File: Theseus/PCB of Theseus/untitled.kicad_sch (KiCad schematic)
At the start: 20 parts, among them J1 TB001-500-04BE, J4 TB003-500-P06BE, J8 TB003-500-P06BE, Q1 NX3020NAK,215, Q2 NX3020NAK,215

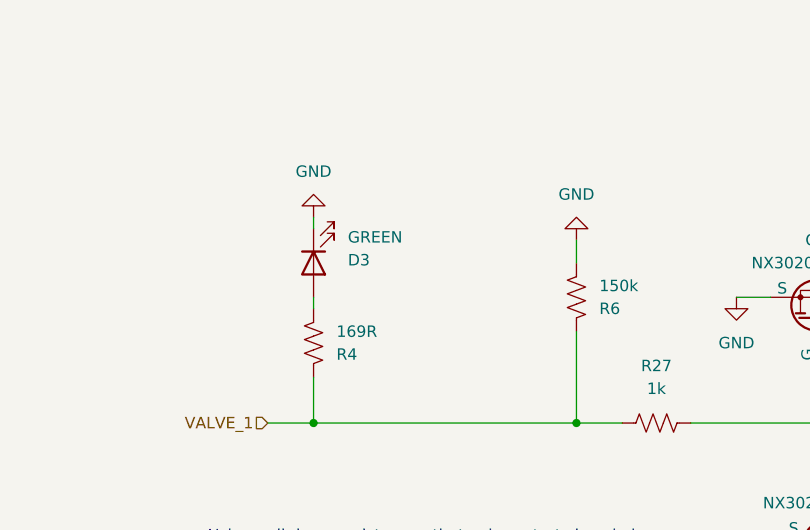
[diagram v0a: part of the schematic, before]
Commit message: Fixes V3
- Copied Ferrite Bead P/N from processor
- Added external oscillator
- Made status LED pins pull-down
- Copied processor programming header
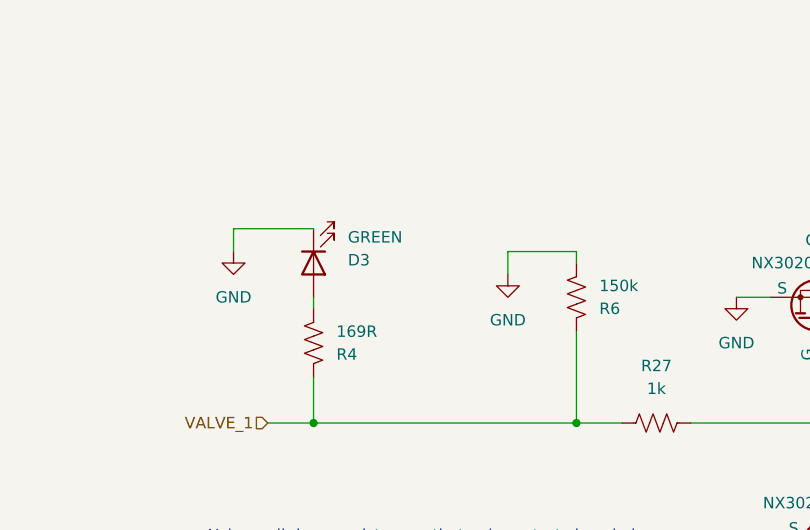
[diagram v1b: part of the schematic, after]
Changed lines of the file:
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@@
 	(wire
 		(pts
-			(xy 180.34 48.26) (xy 180.34 45.72)
+			(xy 172.72 46.99) (xy 172.72 49.53)
 		)
 		(stroke
@@
 	(wire
 		(pts
-			(xy 151.13 43.18) (xy 151.13 44.45)
+			(xy 142.24 46.99) (xy 142.24 44.45)
+		)
+		(stroke
+			(width 0)
+			(type default)
+		)
+	)
+	(wire
+		(pts
+			(xy 142.24 44.45) (xy 151.13 44.45)
 		)
 		(stroke
@@
 	(wire
 		(pts
+			(xy 180.34 46.99) (xy 180.34 48.26)
+		)
+		(stroke
+			(width 0)
+			(type default)
+		)
+	)
+	(wire
+		(pts
 			(xy 219.71 54.61) (xy 219.71 60.96)
 		)
@@
 		(pts
 			(xy 227.33 52.07) (xy 254 52.07)
+		)
+		(stroke
+			(width 0)
+			(type default)
+		)
+	)
+	(wire
+		(pts
+			(xy 172.72 46.99) (xy 180.34 46.99)
 		)
 		(stroke
@@
 	(symbol
 		(lib_id "power:GND")
-		(at 180.34 45.72 0)
-		(mirror x)
+		(at 172.72 49.53 0)
+		(mirror y)
 		(unit 1)
 		(exclude_from_sim no)
@@
 		(on_board yes)
 		(dnp no)
-		(fields_autoplaced yes)
 		(property "Reference" "#PWR06"
-			(at 180.34 39.37 0)
+			(at 172.72 55.88 0)
 			(effects
 				(font
@@
 		)
 		(property "Value" "GND"
-			(at 180.34 40.64 0)
+			(at 172.72 54.61 0)
 			(effects
 				(font
@@
 		)
 		(property "Footprint" ""
-			(at 180.34 45.72 0)
+			(at 172.72 49.53 0)
 			(effects
 				(font
@@
 		)
 		(property "Datasheet" ""
-			(at 180.34 45.72 0)
+			(at 172.72 49.53 0)
 			(effects
 				(font
@@
 		)
 		(property "Description" "Power symbol creates a global label with name \"GND\" , ground"
-			(at 180.34 45.72 0)
+			(at 172.72 49.53 0)
 			(effects
 				(font
@@
 	(symbol
 		(lib_id "power:GND")
-		(at 151.13 43.18 0)
-		(mirror x)
+		(at 142.24 46.99 0)
 		(unit 1)
 		(exclude_from_sim no)
@@
 		(on_board yes)
 		(dnp no)
-		(fields_autoplaced yes)
 		(property "Reference" "#PWR012"
-			(at 151.13 36.83 0)
+			(at 142.24 53.34 0)
 			(effects
 				(font
@@
 		)
 		(property "Value" "GND"
-			(at 151.13 38.1 0)
+			(at 142.24 52.07 0)
 			(effects
 				(font
@@
 		)
 		(property "Footprint" ""
-			(at 151.13 43.18 0)
+			(at 142.24 46.99 0)
 			(effects
 				(font
@@
 		)
 		(property "Datasheet" ""
-			(at 151.13 43.18 0)
+			(at 142.24 46.99 0)
 			(effects
 				(font
@@
 		)
 		(property "Description" "Power symbol creates a global label with name \"GND\" , ground"
-			(at 151.13 43.18 0)
-			(effects
-				(font
+			(at 142.24 46.99 0)
+			(effects
+				(font

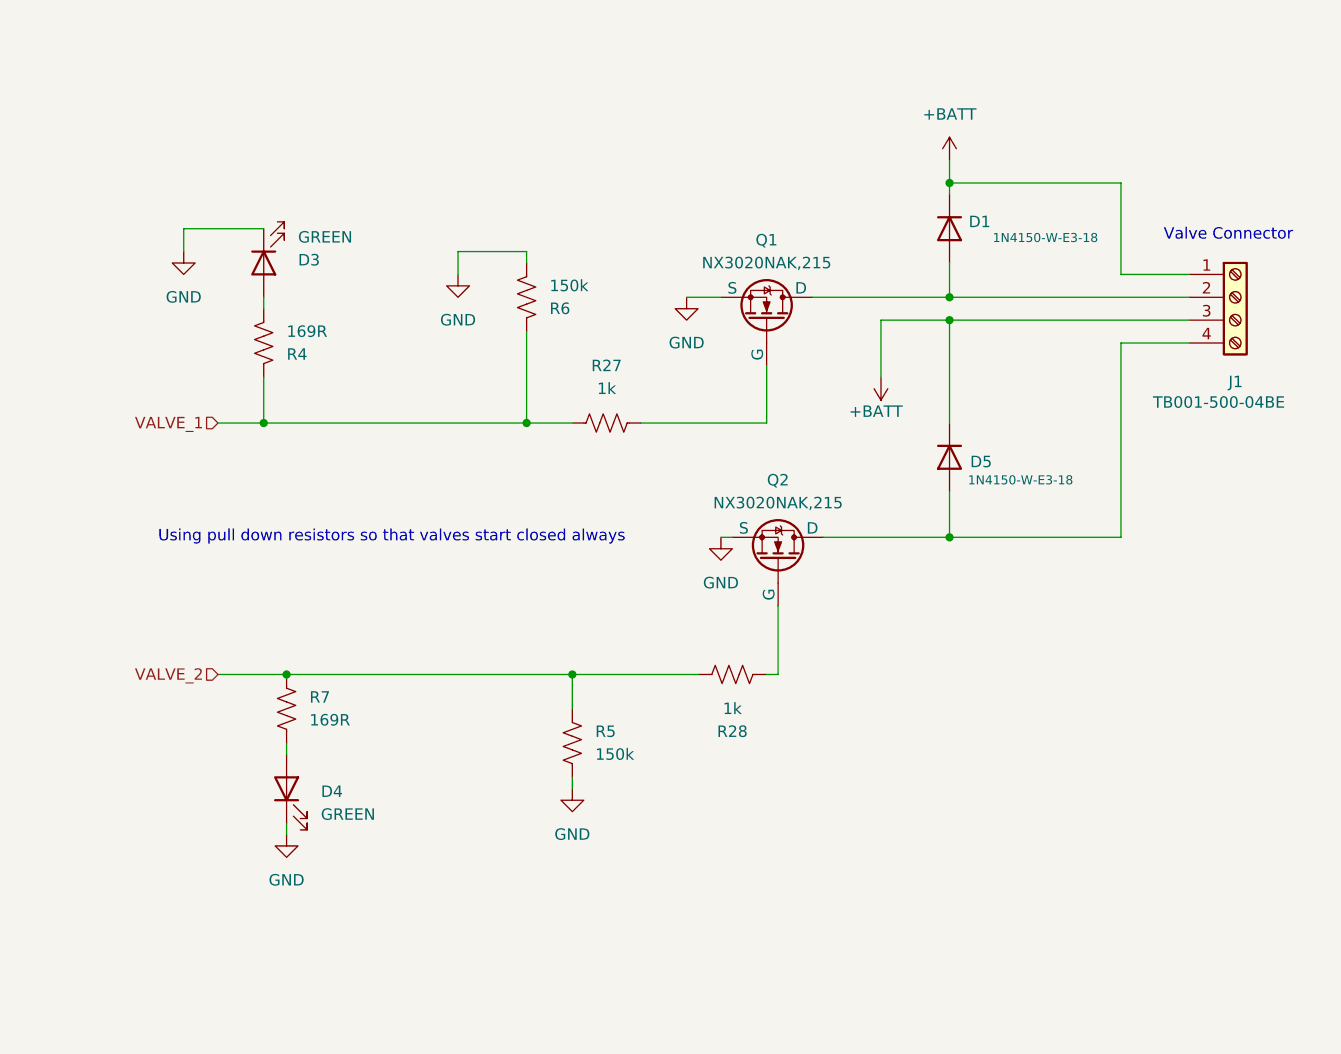
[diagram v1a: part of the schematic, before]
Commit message: NMOS and Diode Update
Updated Diode and NMOS to support 1A max. Fixed valve state LED to draw from BATT instead of MCU.
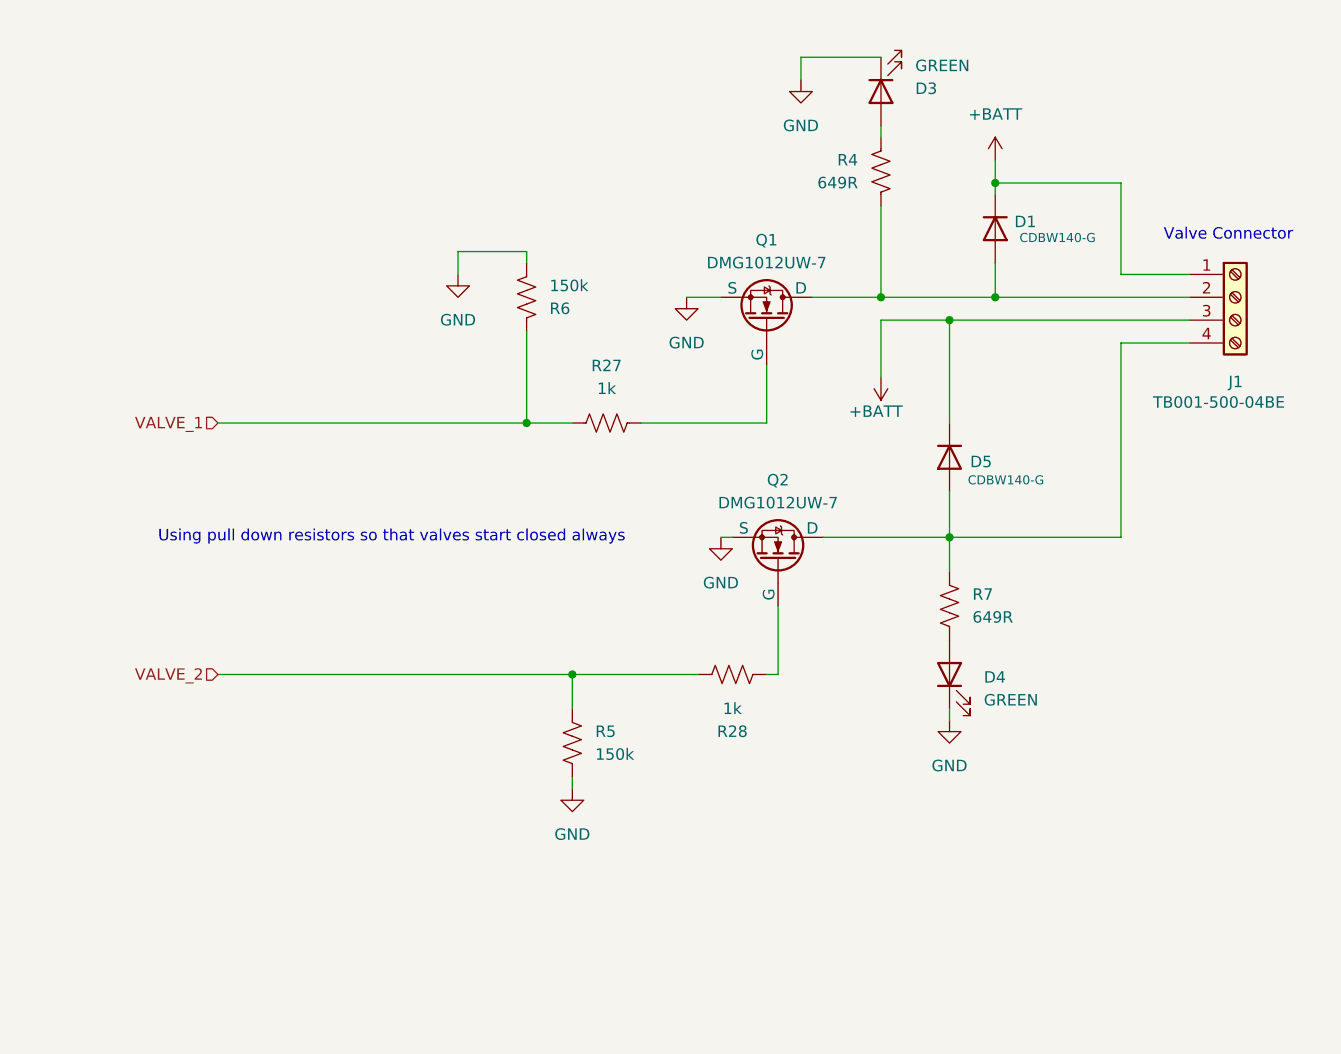
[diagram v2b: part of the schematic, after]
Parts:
- D1, D5: value 1N4150-W-E3-18 -> CDBW140-G
- Q1, Q2: value NX3020NAK,215 -> DMG1012UW-7; footprint Package_TO_SOT_SMD:SOT-23-3 -> Package_TO_SOT_SMD:SOT-323_SC-70_Handsoldering
- R4, R7: value 169R -> 649R
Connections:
- net VALVE_1: no longer R4.1
- net VALVE_2: no longer R7.1
- net at D1.2 (A), J1.2 (Pin_2), Q1.1 (D): now also R4.1
- net at D5.2 (A), J1.4 (Pin_4), Q2.1 (D): now also R7.1
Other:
- moved on the sheet: D1, D3, D4, R4, R7

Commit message: Flight design, first pass
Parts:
- removed J1: TB001-500-04BE, TerminalBlock_CUI:TerminalBlock_CUI_TB007-508-04_1x04_P5.08mm_Horizontal, symbol Connector:Screw_Terminal_01x04
- removed J4, J8: TB003-500-P06BE, TerminalBlock_CUI:TerminalBlock_CUI_TB007-508-06_1x06_P5.08mm_Horizontal, symbol Connector:Screw_Terminal_01x06
- added C35: 0.1u, Capacitor_SMD:C_0805_2012Metric_Pad1.18x1.45mm_HandSolder, symbol Device:C
- added J1, J2, J4: Conn_01x06_Socket, canhw_footprints:connector_Harwin_G125–MG10605M4P, symbol Connector:Conn_01x06_Socket
- added TP4: TC1+, TestPoint:TestPoint_Pad_D2.0mm, symbol Connector:TestPoint
- added TP5: TC1-, TestPoint:TestPoint_Pad_D2.0mm, symbol Connector:TestPoint
- added U13: MAX6675, Package_SO:SOIC-8_3.9x4.9mm_P1.27mm, symbol FYDP_Library:MAX6675
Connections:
- net +3.3V: now also C35.1, J2.1 (Pin_1), J2.4 (Pin_4), U13.4 (Vcc)
- net +BATT: now also J1.1 (Pin_1), J1.3 (Pin_3), J4.1 (Pin_1), J4.3 (Pin_3), J4.5 (Pin_5)
- net GND: now also C35.2, J2.3 (Pin_3), J2.6 (Pin_6), U13.1 (GND)
- net HALL_1: now also J2.2 (Pin_2)
- net HALL_2: now also J2.5 (Pin_5)
- net PT1: now also J4.2 (Pin_2)
- net PT2: now also J4.4 (Pin_4)
- net PT3: now also J4.6 (Pin_6)
- net at D1.2 (A), Q1.1 (D), R4.1: now also J1.2 (Pin_2)
- net at D5.2 (A), Q2.1 (D), R7.1: now also J1.4 (Pin_4)
- new net TC1+: J1.5 (Pin_5), TP4.1, U13.2 (T-)
- new net TC1-: J1.6 (Pin_6), TP5.1, U13.3 (T+)
- new net TC1_CS: U13.6 (~{CS})
- new net TC1_SCK: U13.5 (SCK)
- new net TC1_SO: U13.7 (SO)
- no-connect marks 0 -> 1
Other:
- note added: "1x 0.1u for MAX6675"
- note added: "TC1, COTS OPTION"
- note added: "Valve + TC Connector"
- note removed: "Valve Connector"

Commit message: Flight design v1
First pass at flight design
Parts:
- removed J4: Conn_01x06_Socket, canhw_footprints:connector_Harwin_G125–MG10605M4P, symbol Connector:Conn_01x06_Socket
- added J8: Conn_01x12_Socket, canhw_footprints:connector_Harwin_G125-MV11205M1P, symbol Connector:Conn_01x12_Socket
- added R10, R19, R8: 82K, Resistor_SMD:R_0603_1608Metric_Pad0.98x0.95mm_HandSolder, symbol Device:R_US
- added R18, R20, R9: 130K, Resistor_SMD:R_0603_1608Metric_Pad0.98x0.95mm_HandSolder, symbol Device:R_US
- C18, C19, C35: footprint Capacitor_SMD:C_0805_2012Metric_Pad1.18x1.45mm_HandSolder -> Capacitor_SMD:C_0603_1608Metric_Pad1.08x0.95mm_HandSolder
- R1, R2, R27, R28, R3, R4, R5, R6, R7: footprint Resistor_SMD:R_0805_2012Metric_Pad1.20x1.40mm_HandSolder -> Resistor_SMD:R_0603_1608Metric_Pad0.98x0.95mm_HandSolder
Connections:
- net +BATT: now also J8.7 (Pin_7), J8.8 (Pin_8), J8.9 (Pin_9)
- net GND: now also J8.10 (Pin_10), J8.11 (Pin_11), J8.12 (Pin_12), R18.2, R20.2, R9.2
- net PT1: now also J8.4 (Pin_4)
- net PT2: now also J8.5 (Pin_5)
- net PT3: now also J8.6 (Pin_6)
- new net PT4: R8.2, R9.1
- new net PT4_OUT: J8.1 (Pin_1), R8.1
- new net PT5: R10.2, R18.1
- new net PT5_OUT: J8.2 (Pin_2), R10.1
- new net PT6: R19.2, R20.1
- new net PT6_OUT: J8.3 (Pin_3), R19.1
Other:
- note added: "CURRENT PTs: Scaling 4-20 mA to 0.6-3V"
- note added: "VOLTAGE PTS: Divide-by-1.631 scales 0-5V output to 0-3.066V"
- note added: "Voltage PTs pins 1-3 Current PTs pins 4-6"
- note removed: "Pressure Transducer Connector"
- note removed: "Scaling 4-20 mA to 0.6-3V"
- moved on the sheet: C35, D1, D3, D4, D5, J1, Q1, Q2, R27, R28, R4, R5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

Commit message: 10 MAR 2026 Changes pt 2
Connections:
- net GND: now also J1.6 (Pin_6), TP5.1, U13.2 (T-)
- net TC1+: now also U13.3 (T+); no longer U13.2 (T-)
- removed net TC1-: J1.6 (Pin_6), TP5.1, U13.3 (T+)
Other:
- note added: "https://www.analog.com/media/en/technical-documentation/data-sheets/MAX6675.pdf"
- note added: "https://www.diodes.com/assets/Datasheets/DMG1012UW.pdf"
- moved on the sheet: TP4, TP5, U13

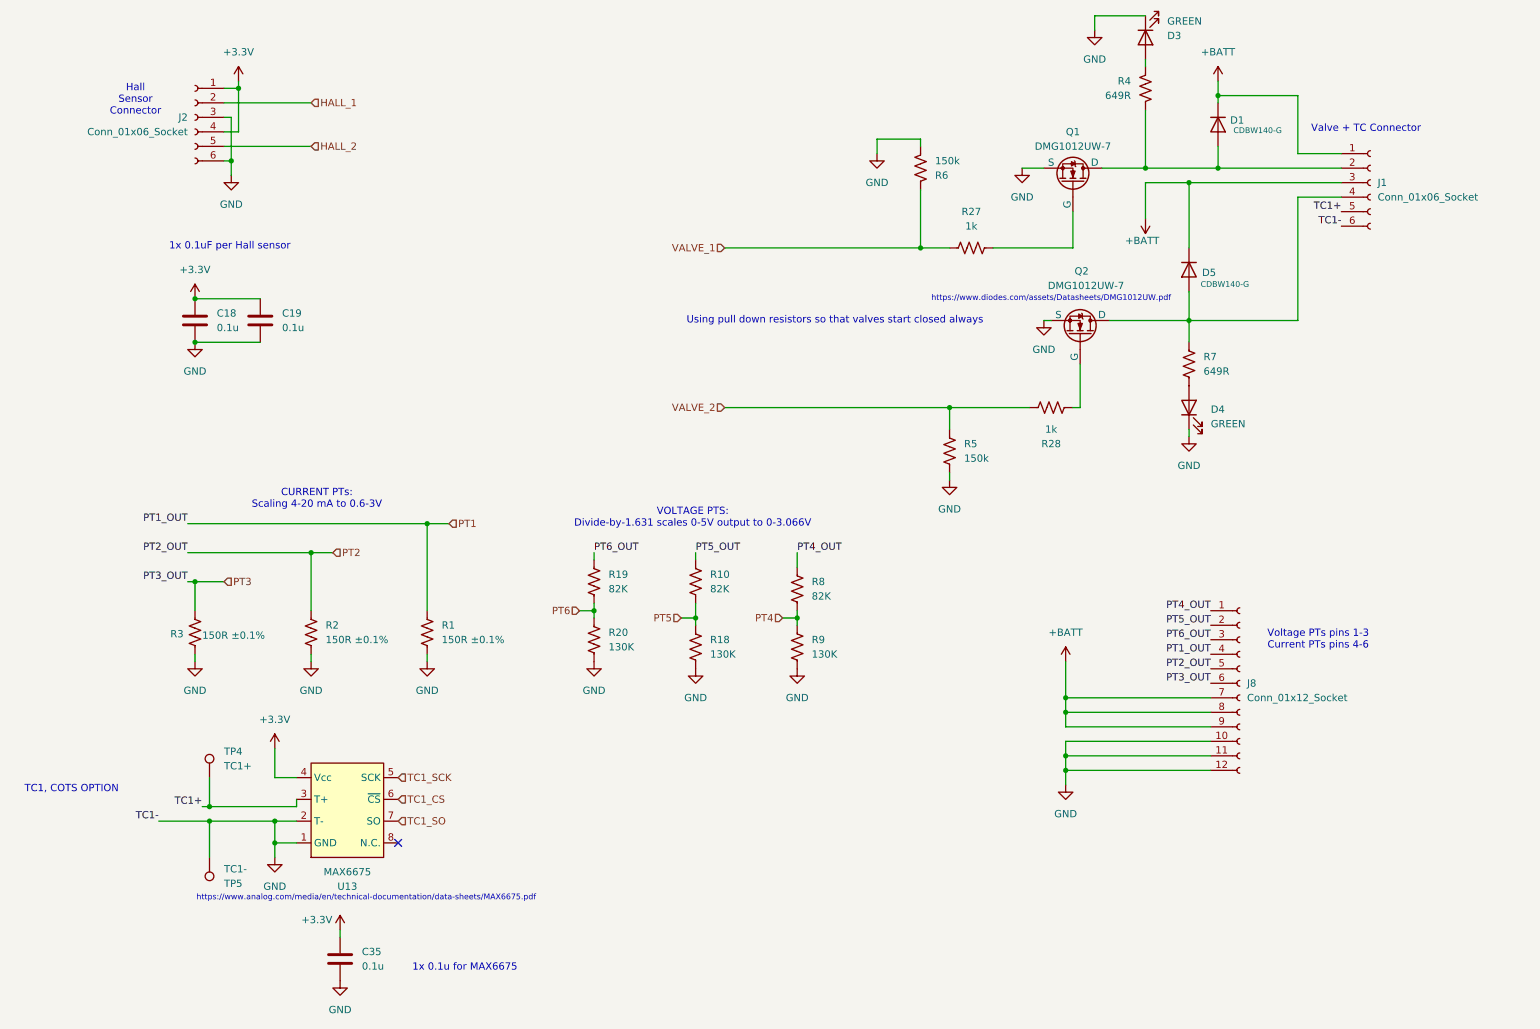
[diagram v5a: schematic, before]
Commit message: change CAN transciever to 3v3, add lipo charging, change PT connectors, tidy schematic
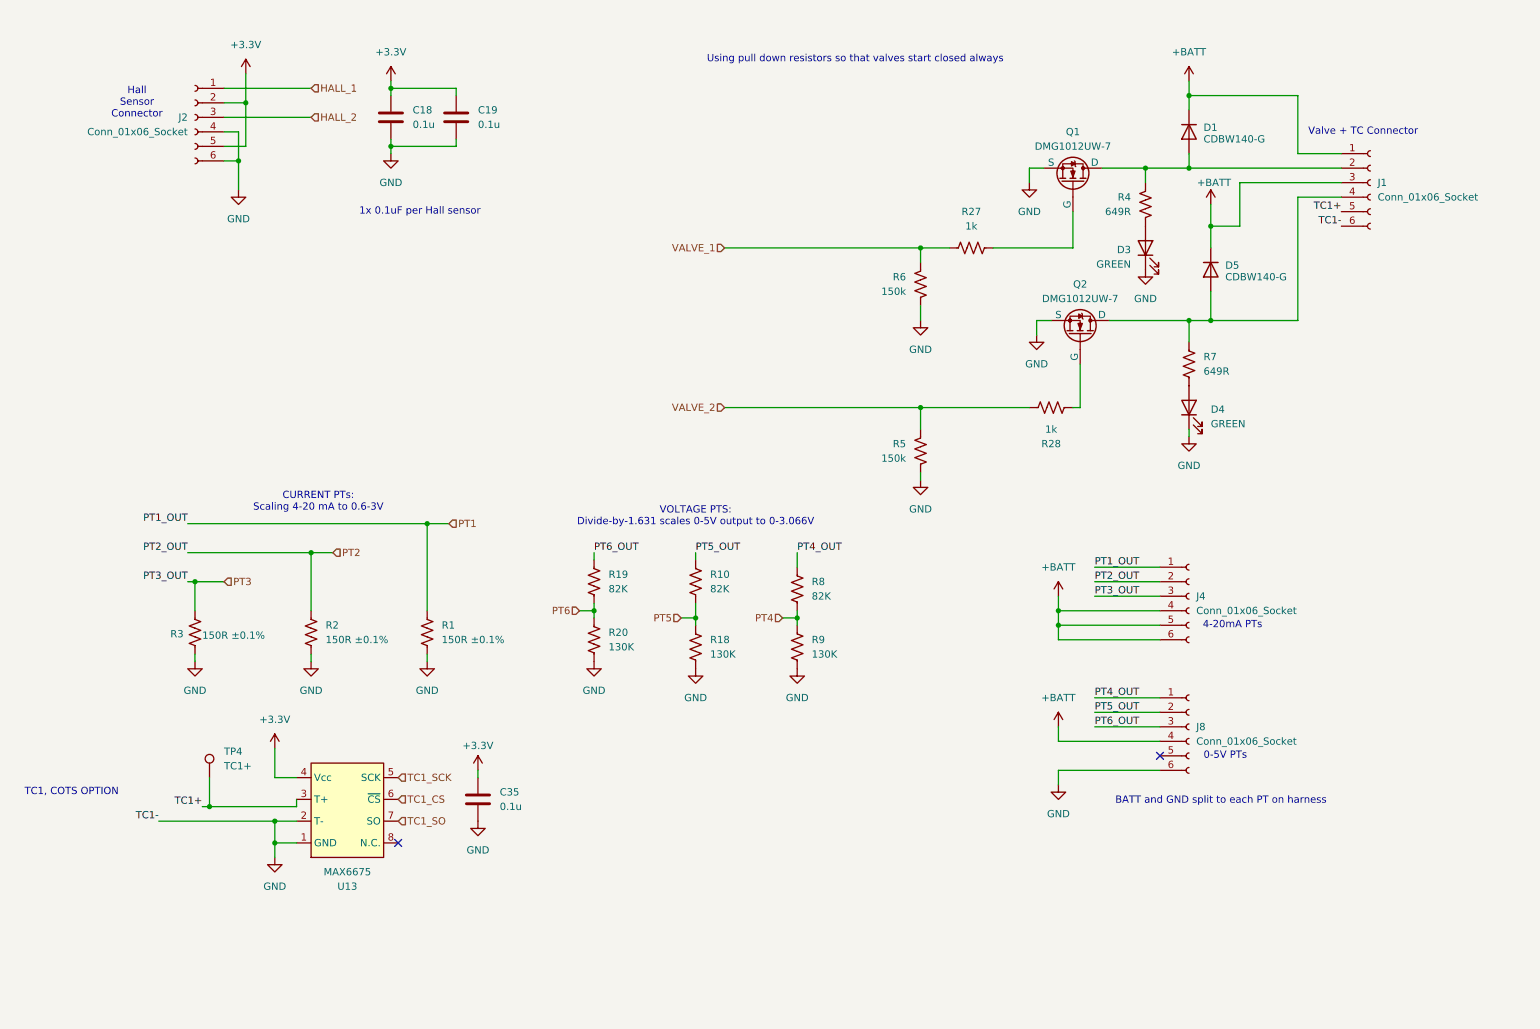
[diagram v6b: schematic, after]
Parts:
- removed J8: Conn_01x12_Socket, canhw_footprints:connector_Harwin_G125-MV11205M1P, symbol Connector:Conn_01x12_Socket
- removed TP5: TC1-, TestPoint:TestPoint_Pad_D2.0mm, symbol Connector:TestPoint
- added J4, J8: Conn_01x06_Socket, canhw_footprints:connector_Harwin_G125–MG10605M4P, symbol Connector:Conn_01x06_Socket
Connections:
- net +3.3V: now also J2.2 (Pin_2), J2.5 (Pin_5); no longer J2.1 (Pin_1), J2.4 (Pin_4)
- net +BATT: now also J4.4 (Pin_4), J4.5 (Pin_5), J4.6 (Pin_6), J8.4 (Pin_4)
- net GND: now also J2.4 (Pin_4), R6.1, J8.6 (Pin_6); no longer J2.3 (Pin_3), R6.2
- net HALL_1: now also J2.1 (Pin_1); no longer J2.2 (Pin_2)
- net HALL_2: now also J2.3 (Pin_3); no longer J2.5 (Pin_5)
- net PT1: now also J4.1 (Pin_1)
- net PT2: now also J4.2 (Pin_2)
- net PT3: now also J4.3 (Pin_3)
- net PT4_OUT: now also J8.1 (Pin_1)
- net PT5_OUT: now also J8.2 (Pin_2)
- net PT6_OUT: now also J8.3 (Pin_3)
- net VALVE_1: now also R6.2; no longer R6.1
- net at D1.2 (A), J1.2 (Pin_2), Q1.1 (D): now also R4.2; no longer R4.1
- net at D3.2 (A): now also R4.1; no longer R4.2
- no-connect marks 1 -> 2
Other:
- note added: "0-5V PTs"
- note added: "4-20mA PTs"
- note added: "BATT and GND split to each PT on harness"
- note removed: "1x 0.1u for MAX6675"
- note removed: "Voltage PTs pins 1-3 Current PTs pins 4-6"
- note removed: "https://www.analog.com/media/en/technical-documentation/data-sheets/MAX6675.pdf"
- note removed: "https://www.diodes.com/assets/Datasheets/DMG1012UW.pdf"
- moved on the sheet: C18, C19, C35, D3, D5, R4, R5, R6
